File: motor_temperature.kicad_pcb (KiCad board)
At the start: 2 copper layers, 75.2 x 53.6 mm, 18 parts, among them J1 TBL002A-350-03GR-2OR, J2 TBL002A-350-03GR-2OR, J3 TBL002A-350-03GR-2OR, U1 DRV8870DDA, U2 L9110S, U3 TMP144YFFR, U4 TMP75AIDR

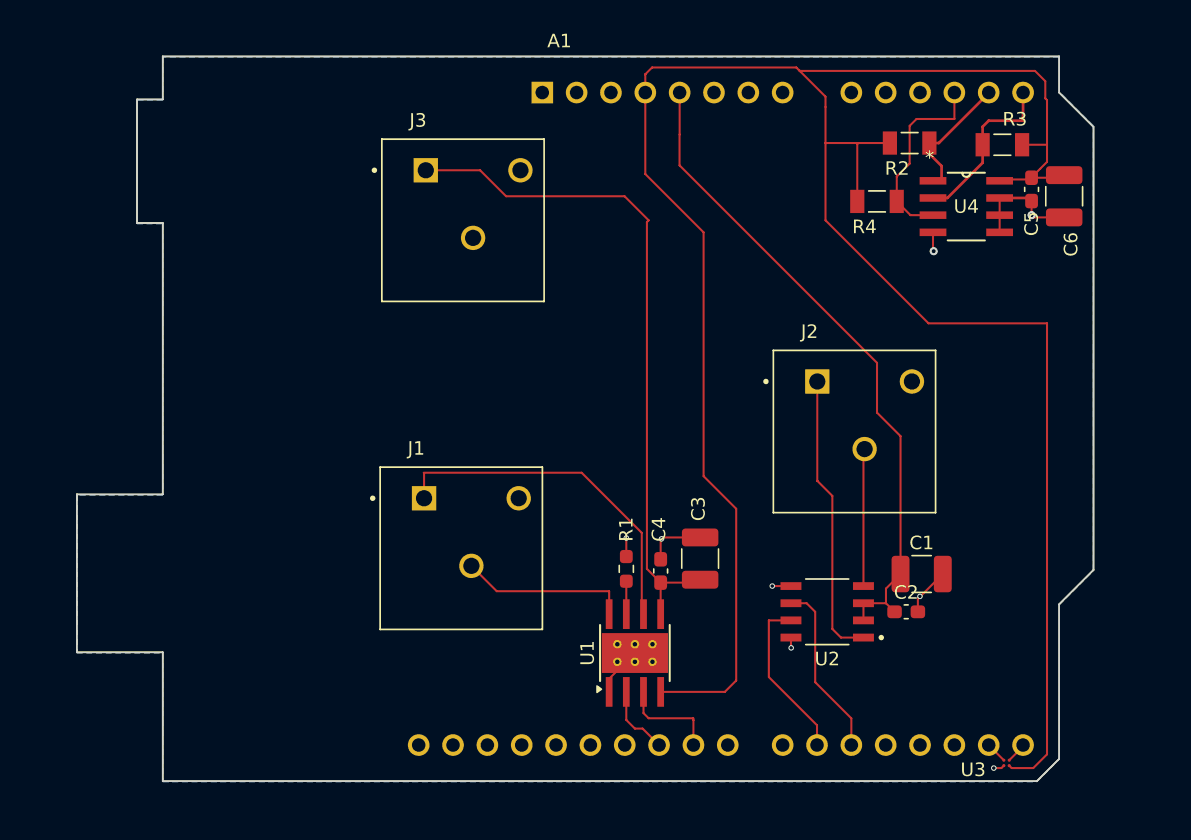
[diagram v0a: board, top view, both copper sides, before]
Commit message: Incorporated feedback
1) Flipped Arduino template for shield to correctly match the STM32 Dicovery board. Rerouted the circuit modules.
2) Labeled terminals
3) Removed unnecessary tabs
4) Added trace for Tachometer with 0 Ohm resistor
5) Resolved all DRC issues related to silkscreen and clearance
6) Generated Gerbers, drill files and BOM
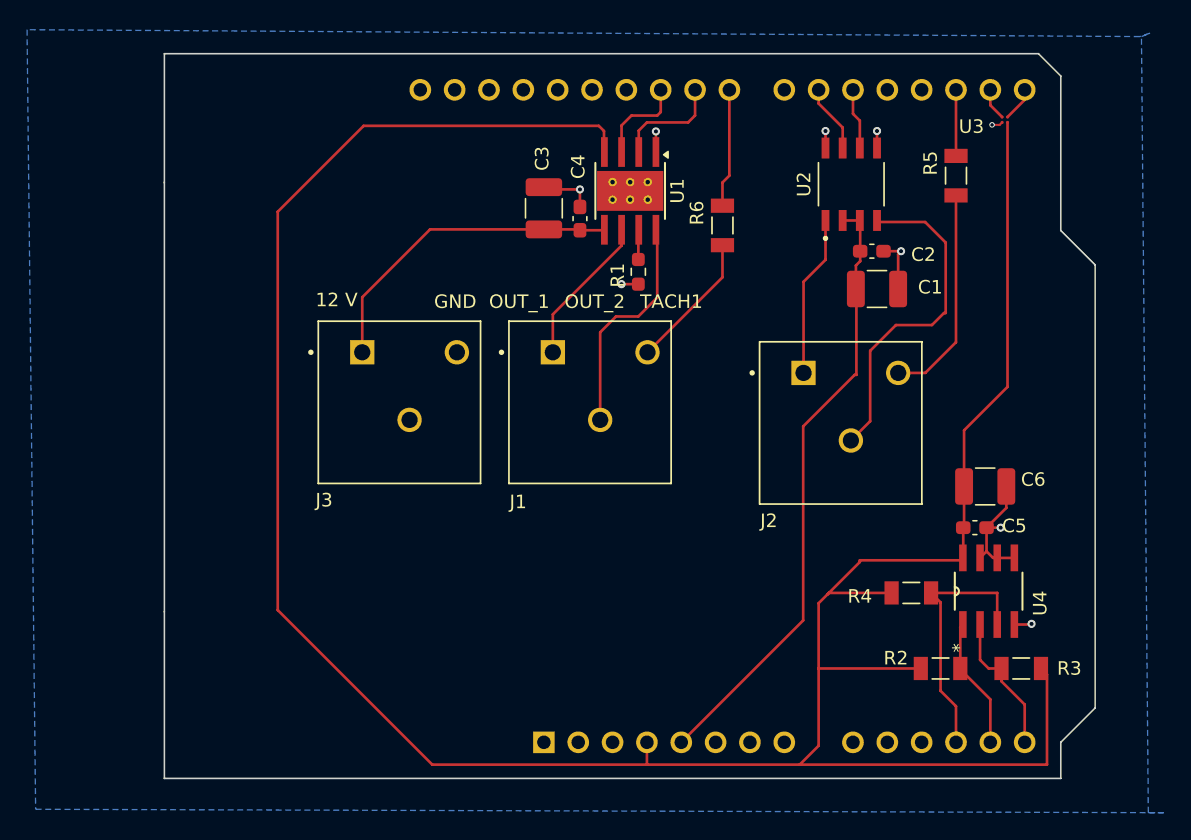
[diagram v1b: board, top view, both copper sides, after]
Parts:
- added R5: 0R, 1206W4F0000T5E:RESC3115X65N, F.Cu at (156.8, 72.5)
- added R6: 0R, 1206W4F0000T5E:RESC3115X65N, F.Cu at (139.6, 76.2)
- A1: footprint Module:Arduino_UNO_R3_edgecuts_withoutcourtyard -> Module:Arduino_UNO_R3_edgecuts_withoutcourtyard_notabs_nosilkscreern; moved to B.Cu
- moved A1 48.1 mm to (126.4, 114.4)
- moved U3 47.6 mm to (160.5, 68.4)
- moved R2 38.9 mm to (155.7, 109.0)
- moved R3 38.8 mm to (161.7, 109.0)
- moved U1 34.2 mm to (132.7, 73.6), turned to -90 degrees
- moved U2 31.7 mm to (149.1, 73.2), turned to 90 degrees
- moved R4 29.1 mm to (153.5, 103.4)
- moved U4 28.5 mm to (159.3, 103.3), turned to 90 degrees
- moved C3 28.4 mm to (126.4, 74.9)
- moved C2 26.8 mm to (150.6, 78.1)
- moved C4 26.7 mm to (129.0, 75.7)
- moved C5 25.4 mm to (158.2, 98.6), turned to 0 degrees
- moved C6 22.2 mm to (159.0, 95.5), turned to 0 degrees
- moved R1 22.0 mm to (133.3, 79.6), turned to -90 degrees
- moved C1 21.3 mm to (151.0, 80.9)
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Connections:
- net /3V3 renamed /UART_3V3
- net Net-(U2-OB) renamed /OUT_B
- A1 pad 17: unconnected-(A1-D2-Pad17) -> /TACHCb
- A1 pad 23: unconnected-(A1-D8-Pad23) -> /TACH1b
- A1 pad 24: /IN_1 -> /IN_2
- A1 pad 25: /IN_2 -> /IN_1
- J1 pad 3: unconnected-(J1-Pad3) -> /TACH1a
- J2 pad 3: unconnected-(J2-Pad3) -> /TACHCa
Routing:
- net +12V: track 50.6 -> 24.1 mm
- net /UART_3V3: track 173.3 -> 199.1 mm
- net /TACHCa: track 0.00 -> 16.1 mm
- net /OUT_B: track 10.2 -> 24.9 mm
- net /OUT_1: track 25.9 -> 11.2 mm
- net /TACH1a: track 0.00 -> 10.2 mm
- net /OUT_A: track 21.3 -> 11.9 mm
- net /TACH1b: track 0.00 -> 8.79 mm
- net /IN_A: track 13.0 -> 4.52 mm
- net /IN_B: track 12.3 -> 5.04 mm
- net /TACHCb: track 0.00 -> 4.89 mm
- net /ALERT: track 14.6 -> 19.0 mm
- net /OUT_2: track 12.7 -> 16.8 mm
- net +5V: track 48.8 -> 45.5 mm
- net /IN_2: track 5.27 -> 8.11 mm
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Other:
- board size 75.2 x 53.6 mm -> 68.8 x 53.6 mm
- board text added: "12 V"
- board text added: "GND"
- board text added: "OUT_1"
- board text added: "OUT_2"
- board text added: "TACH1"
